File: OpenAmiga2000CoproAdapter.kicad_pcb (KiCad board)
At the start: 2 copper layers, 188.6 x 110.4 mm, 75 parts, among them CN1 A2000_COPRO_SLOT, P1 CONN_2, P10 CONN_1, P11 CONN_1, P12 CONN_1, P13 CONN_1, P14 CONN_1, P15 CONN_1, P2 CONN_2, P3 CONN_2, P4 CONN_2, P5 CONN_1, P6 CONN_1, P7 CONN_1, P8 CONN_1, P9 CONN_1, P99 OSHW_LOGO, U1 68000D, U10 Spare, U11 74HCT00, U12 74HCT27, U13 74HCT74, U14 74F86, U15 74F74, U16 74HCT04, U17 74HCT112, U18 74F157, U19 74F157, U2 AS6C4008-55PCN, U3 AS6C4008-55PCN, U4 AS6C4008-55PCN, U5 AS6C4008-55PCN, U6 74HCT00, U7 74HCT32, U8 74HCT32, U9 74LS05

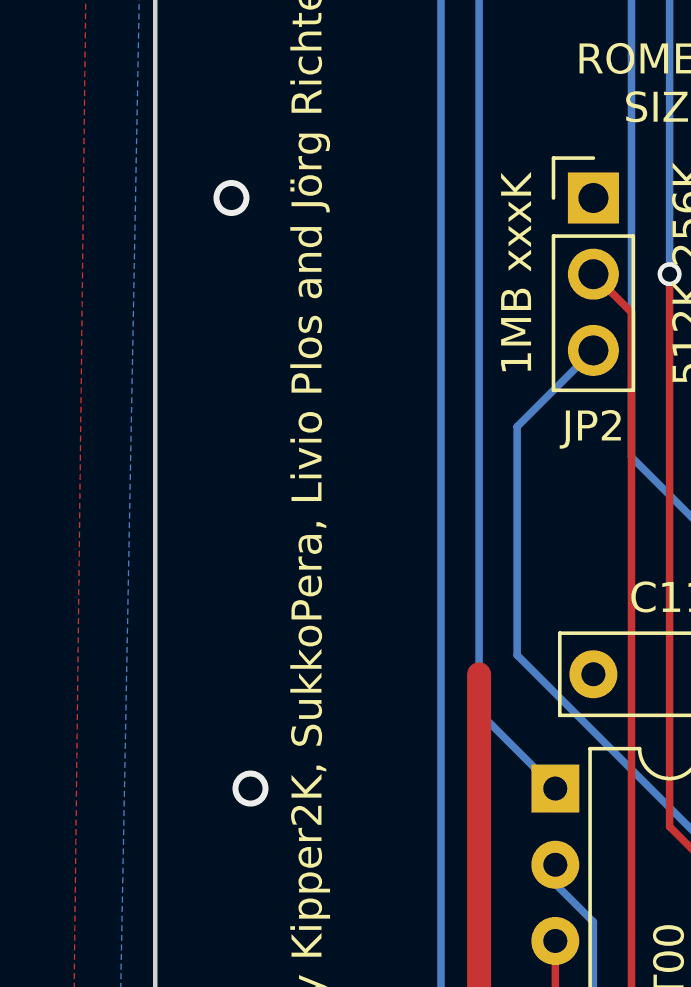
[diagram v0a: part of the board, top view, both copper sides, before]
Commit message: fix unconnected via
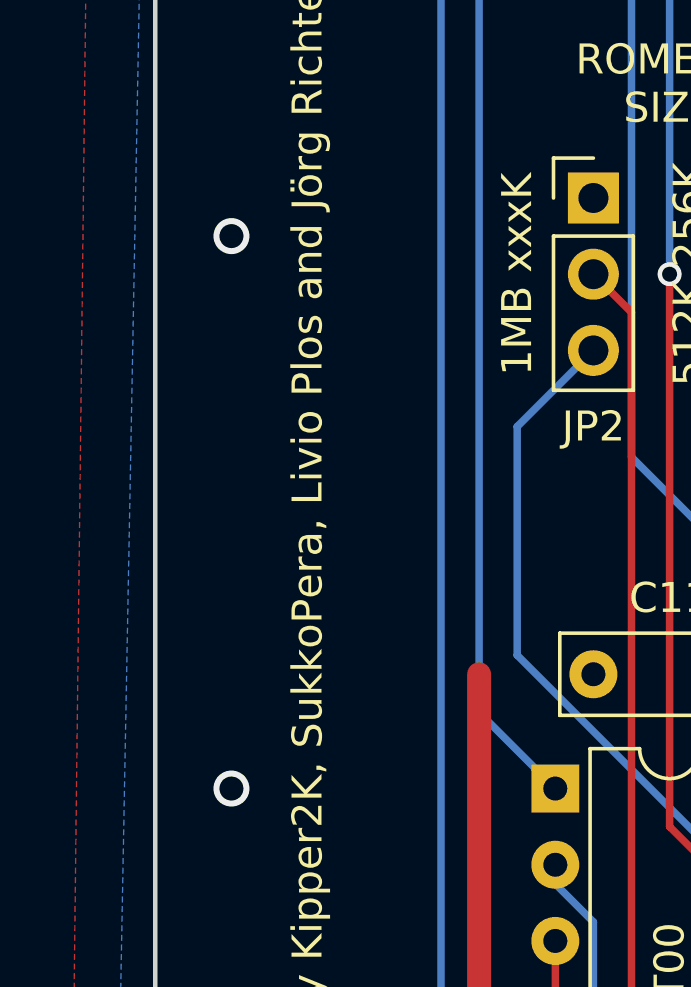
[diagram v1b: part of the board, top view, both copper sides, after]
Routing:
- net GND: vias 173 -> 174
- net (no net): vias 1 -> 0
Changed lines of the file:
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@@
   (gr_line (start 202.3745 139.0015) (end 202.3745 145.9865) (layer Edge.Cuts) (width 0.15))
   (gr_line (start 90.7415 145.9865) (end 90.7415 139.0904) (layer Edge.Cuts) (width 0.15))
-  (via (at 43.7515 72.39) (size 1.2) (drill 0.8) (layers F.Cu B.Cu) (net 0))
   (segment (start 80.8965 50.8) (end 77.7215 47.625) (width 0.25) (layer F.Cu) (net 131))
   (segment (start 82.4865 50.8) (end 80.8965 50.8) (width 0.25) (layer F.Cu) (net 131))
@@
   (via (at 44.3865 137.16) (size 1.2) (drill 0.8) (layers F.Cu B.Cu) (net 1))
   (via (at 44.3865 111.125) (size 1.2) (drill 0.8) (layers F.Cu B.Cu) (net 1))
-  (via (at 44.3865 92.075) (size 1.2) (drill 0.8) (layers F.Cu B.Cu) (net 1))
+  (via (at 43.7515 92.075) (size 1.2) (drill 0.8) (layers F.Cu B.Cu) (net 1))
   (via (at 208.8515 52.705) (size 1.2) (drill 0.8) (layers F.Cu B.Cu) (net 1))
   (via (at 205.0415 57.785) (size 1.2) (drill 0.8) (layers F.Cu B.Cu) (net 1))
@@
   (segment (start 187.2615 122.555) (end 187.2615 127.635) (width 0.8) (layer B.Cu) (net 1))
   (via (at 187.2615 127.635) (size 1.2) (drill 0.8) (layers F.Cu B.Cu) (net 1))
+  (via (at 43.7515 73.66) (size 1.2) (drill 0.8) (layers F.Cu B.Cu) (net 1))
   (segment (start 126.238 108.6485) (end 126.3015 108.585) (width 0.8) (layer F.Cu) (net 2))
   (segment (start 126.238 112.0775) (end 126.238 108.6485) (width 0.8) (layer F.Cu) (net 2))

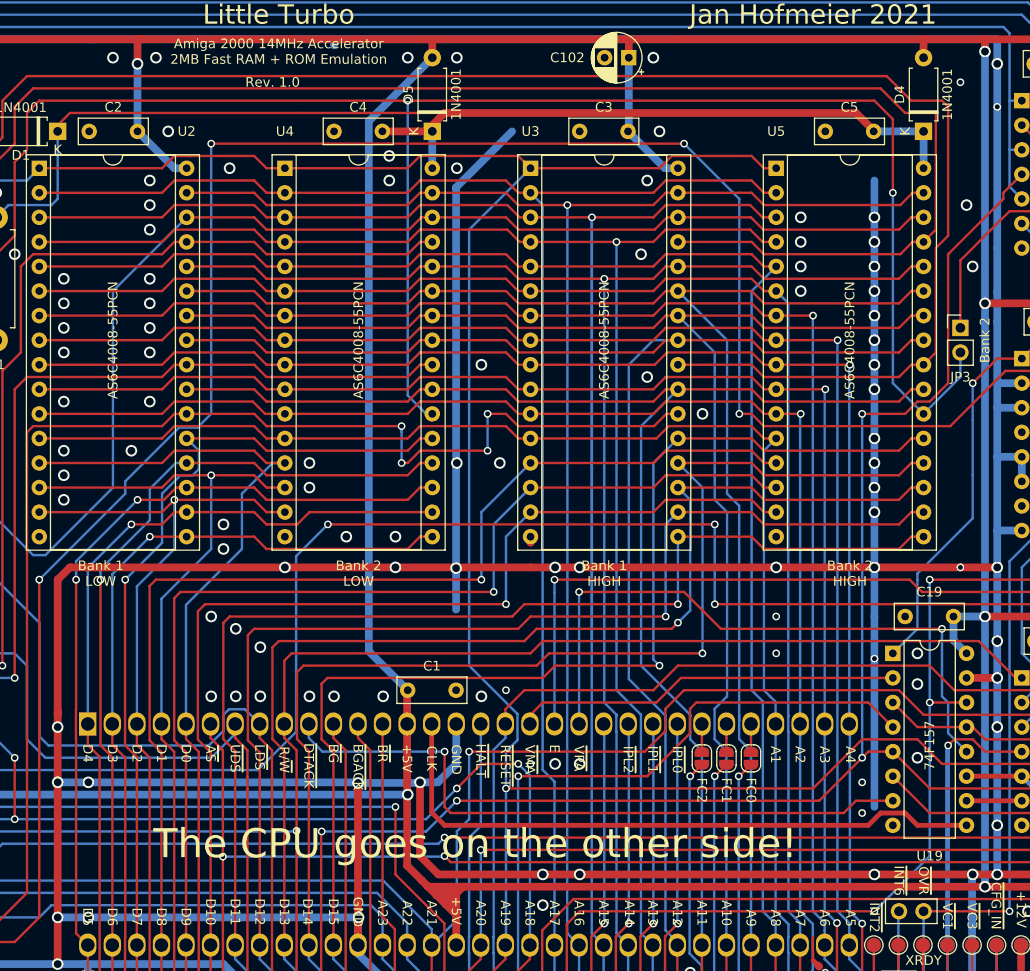
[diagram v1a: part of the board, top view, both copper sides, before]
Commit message: remove a few vias via
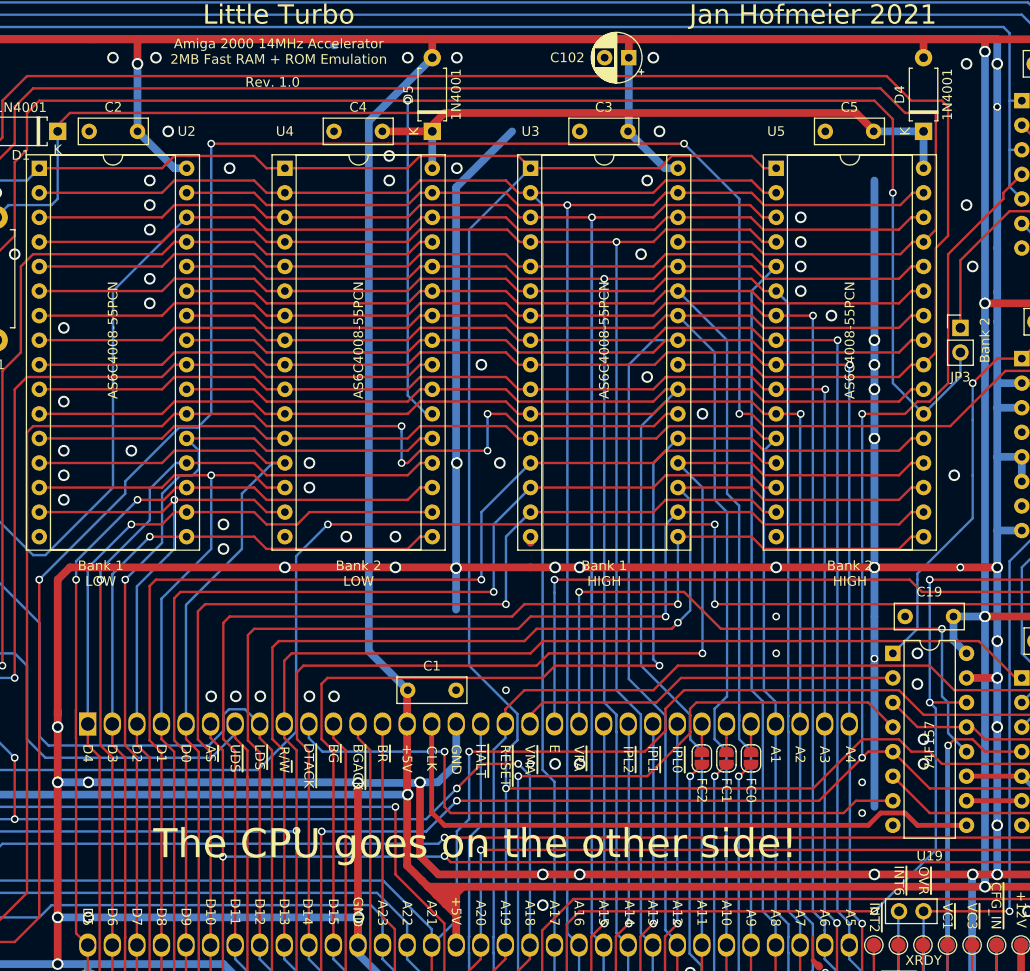
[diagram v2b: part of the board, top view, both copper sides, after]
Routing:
- net /~vpa: track 134.8 -> 135.3 mm
- net GND: vias 174 -> 158
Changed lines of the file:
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@@
     (thickness 1.6)
     (drawings 129)
-    (tracks 2324)
+    (tracks 2311)
     (zones 0)
     (modules 75)
@@
   (via (at 69.7865 111.125) (size 1.2) (drill 0.8) (layers F.Cu B.Cu) (net 1))
   (segment (start 187.2615 103.505) (end 187.2615 103.505) (width 0.8) (layer F.Cu) (net 1))
-  (via (at 187.2615 103.505) (size 1.2) (drill 0.8) (layers F.Cu B.Cu) (net 1))
+  (via (at 187.2615 103.505) (size 1.2) (drill 0.8) (layers F.Cu B.Cu) (net 1) (status 1000000))
   (segment (start 189.8015 86.995) (end 189.8015 84.455) (width 0.8) (layer B.Cu) (net 1))
   (segment (start 187.2615 84.455) (end 189.8015 84.455) (width 0.8) (layer B.Cu) (net 1))
@@
   (via (at 100.2665 43.18) (size 1.2) (drill 0.8) (layers F.Cu B.Cu) (net 1))
   (via (at 166.9415 59.69) (size 1.2) (drill 0.8) (layers F.Cu B.Cu) (net 1))
-  (via (at 174.5615 59.69) (size 1.2) (drill 0.8) (layers F.Cu B.Cu) (net 1))
   (via (at 166.9415 62.23) (size 1.2) (drill 0.8) (layers F.Cu B.Cu) (net 1))
-  (via (at 174.5615 62.23) (size 1.2) (drill 0.8) (layers F.Cu B.Cu) (net 1))
-  (via (at 174.5615 64.77) (size 1.2) (drill 0.8) (layers F.Cu B.Cu) (net 1))
   (via (at 166.9415 64.77) (size 1.2) (drill 0.8) (layers F.Cu B.Cu) (net 1))
   (via (at 166.9415 67.31) (size 1.2) (drill 0.8) (layers F.Cu B.Cu) (net 1))
-  (via (at 174.5615 67.31) (size 1.2) (drill 0.8) (layers F.Cu B.Cu) (net 1))
-  (via (at 174.5615 69.85) (size 1.2) (drill 0.8) (layers F.Cu B.Cu) (net 1))
+  (via (at 170.1165 69.85) (size 1.2) (drill 0.8) (layers F.Cu B.Cu) (net 1))
   (via (at 174.5615 72.39) (size 1.2) (drill 0.8) (layers F.Cu B.Cu) (net 1))
   (via (at 174.5615 74.93) (size 1.2) (drill 0.8) (layers F.Cu B.Cu) (net 1))
   (via (at 174.5615 77.47) (size 1.2) (drill 0.8) (layers F.Cu B.Cu) (net 1))
-  (via (at 174.5615 82.55) (size 1.2) (drill 0.8) (layers F.Cu B.Cu) (net 1))
-  (via (at 174.5615 85.09) (size 1.2) (drill 0.8) (layers F.Cu B.Cu) (net 1))
-  (via (at 174.5615 87.63) (size 1.2) (drill 0.8) (layers F.Cu B.Cu) (net 1))
-  (via (at 174.5615 90.17) (size 1.2) (drill 0.8) (layers F.Cu B.Cu) (net 1))
+  (via (at 182.8165 86.36) (size 1.2) (drill 0.8) (layers F.Cu B.Cu) (net 1))
   (via (at 85.6615 63.5) (size 1.2) (drill 0.8) (layers F.Cu B.Cu) (net 1))
   (via (at 78.0415 97.155) (size 1.2) (drill 0.8) (layers F.Cu B.Cu) (net 1))
   (via (at 118.6815 109.22) (size 1.2) (drill 0.8) (layers F.Cu B.Cu) (net 1))
-  (via (at 123.7615 109.22) (size 1.2) (drill 0.8) (layers F.Cu B.Cu) (net 1))
   (via (at 52.0065 111.125) (size 1.2) (drill 0.8) (layers F.Cu B.Cu) (net 1))
   (via (at 43.7515 54.61) (size 1.2) (drill 0.8) (layers F.Cu B.Cu) (net 1))
@@
   (segment (start 168.2115 136.525) (end 168.2115 135.763425) (width 0.25) (layer F.Cu) (net 1))
   (segment (start 168.2115 135.763425) (end 168.19299 135.744915) (width 0.25) (layer F.Cu) (net 1))
-  (via (at 111.0615 104.14) (size 1.2) (drill 0.8) (layers F.Cu B.Cu) (net 1))
   (via (at 111.0615 109.22) (size 1.2) (drill 0.8) (layers F.Cu B.Cu) (net 1))
-  (via (at 108.5215 102.235) (size 1.2) (drill 0.8) (layers F.Cu B.Cu) (net 1))
   (via (at 108.5215 109.22) (size 1.2) (drill 0.8) (layers F.Cu B.Cu) (net 1))
-  (via (at 105.9815 100.965) (size 1.2) (drill 0.8) (layers F.Cu B.Cu) (net 1))
   (via (at 105.9815 109.22) (size 1.2) (drill 0.8) (layers F.Cu B.Cu) (net 1))
   (via (at 144.0815 95.885) (size 1.2) (drill 0.8) (layers F.Cu B.Cu) (net 1))
@@
   (segment (start 187.2615 48.26) (end 187.2615 62.865) (width 0.8) (layer B.Cu) (net 1))
   (via (at 187.2615 48.26) (size 0.8) (drill 0.5) (layers F.Cu B.Cu) (net 1))
-  (via (at 183.4515 45.72) (size 0.8) (drill 0.5) (layers F.Cu B.Cu) (net 1))
   (via (at 78.0415 57.785) (size 0.8) (drill 0.5) (layers F.Cu B.Cu) (net 1))
   (via (at 65.9765 59.055) (size 0.8) (drill 0.5) (layers F.Cu B.Cu) (net 1))
@@
   (via (at 144.0815 127.635) (size 1.2) (drill 0.8) (layers F.Cu B.Cu) (net 1))
   (via (at 140.2715 130.81) (size 1.2) (drill 0.8) (layers F.Cu B.Cu) (net 1))
-  (via (at 133.9215 109.22) (size 1.2) (drill 0.8) (layers F.Cu B.Cu) (net 1))
   (via (at 213.9315 103.505) (size 1.2) (drill 0.8) (layers F.Cu B.Cu) (net 1))
   (segment (start 213.9315 62.23) (end 213.9315 62.795685) (width 0.8) (layer B.Cu) (net 1))
@@
   (via (at 99.6315 66.04) (size 1.2) (drill 0.8) (layers F.Cu B.Cu) (net 1))
   (via (at 99.6315 68.58) (size 1.2) (drill 0.8) (layers F.Cu B.Cu) (net 1))
-  (via (at 99.6315 71.12) (size 1.2) (drill 0.8) (layers F.Cu B.Cu) (net 1))
-  (via (at 99.6315 73.66) (size 1.2) (drill 0.8) (layers F.Cu B.Cu) (net 1))
-  (via (at 99.6315 78.74) (size 1.2) (drill 0.8) (layers F.Cu B.Cu) (net 1))
   (via (at 97.7265 83.82) (size 1.2) (drill 0.8) (layers F.Cu B.Cu) (net 1))
-  (via (at 90.7415 66.04) (size 1.2) (drill 0.8) (layers F.Cu B.Cu) (net 1))
-  (via (at 90.7415 68.58) (size 1.2) (drill 0.8) (layers F.Cu B.Cu) (net 1))
   (via (at 90.7415 71.12) (size 1.2) (drill 0.8) (layers F.Cu B.Cu) (net 1))
-  (via (at 90.7415 73.66) (size 1.2) (drill 0.8) (layers F.Cu B.Cu) (net 1))
   (via (at 90.7415 78.74) (size 1.2) (drill 0.8) (layers F.Cu B.Cu) (net 1))
   (via (at 90.7415 83.82) (size 1.2) (drill 0.8) (layers F.Cu B.Cu) (net 1))
@@
   (via (at 179.0065 107.95) (size 1.2) (drill 0.8) (layers F.Cu B.Cu) (net 1))
   (via (at 187.2615 112.395) (size 1.2) (drill 0.8) (layers F.Cu B.Cu) (net 1))
-  (via (at 179.0065 115.57) (size 1.2) (drill 0.8) (layers F.Cu B.Cu) (net 1))
+  (via (at 179.6415 116.205) (size 1.2) (drill 0.8) (layers F.Cu B.Cu) (net 1))
   (segment (start 174.5615 120.65) (end 174.5615 105.31999) (width 0.8) (layer B.Cu) (net 1))
   (segment (start 217.7415 103.505) (end 217.7415 100.33) (width 0.8) (layer B.Cu) (net 1))
@@
   (via (at 187.2615 127.635) (size 1.2) (drill 0.8) (layers F.Cu B.Cu) (net 1))
   (via (at 43.7515 73.66) (size 1.2) (drill 0.8) (layers F.Cu B.Cu) (net 1))
+  (via (at 174.5615 82.55) (size 1.2) (drill 0.8) (layers F.Cu B.Cu) (net 1))
+  (via (at 184.0865 43.815) (size 1.2) (drill 0.8) (layers F.Cu B.Cu) (net 1))
+  (via (at 179.6415 113.665) (size 1.2) (drill 0.8) (layers F.Cu B.Cu) (net 1))
   (segment (start 126.238 108.6485) (end 126.3015 108.585) (width 0.8) (layer F.Cu) (net 2))
   (segment (start 126.238 112.0775) (end 126.238 108.6485) (width 0.8) (layer F.Cu) (net 2))
@@
   (segment (start 174.5615 131.445012) (end 144.081488 131.445012) (width 0.25) (layer F.Cu) (net 6))
   (segment (start 174.5615 131.445) (end 174.5615 131.445012) (width 0.25) (layer B.Cu) (net 6))
-  (segment (start 180.276538 125.729962) (end 174.5615 131.445) (width 0.25) (layer B.Cu) (net 6))
-  (segment (start 180.276538 109.855) (end 180.276538 125.729962) (width 0.25) (layer B.Cu) (net 6))
+  (segment (start 180.9115 125.095) (end 174.5615 131.445) (width 0.25) (layer B.Cu) (net 6))
+  (segment (start 180.9115 110.489962) (end 180.9115 125.095) (width 0.25) (layer B.Cu) (net 6))
+  (segment (start 180.276538 109.855) (end 180.9115 110.489962) (width 0.25) (layer B.Cu) (net 6))
   (segment (start 140.208 133.4135) (end 143.4465 130.175) (width 0.25) (layer F.Cu) (net 7))
   (segment (start 143.4465 130.175) (end 192.9765 130.175) (width 0.25) (layer F.Cu) (net 7))
@@
   (segment (start 63.4365 55.88) (end 58.3565 60.96) (width 0.25) (layer B.Cu) (net 11))
   (segment (start 86.9315 55.88) (end 63.4365 55.88) (width 0.25) (layer B.Cu) (net 11))
+  (segment (start 173.2915 113.665) (end 168.2115 118.745) (width 0.25) (layer F.Cu) (net 11))
+  (segment (start 177.1015 113.665) (end 173.2915 113.665) (width 0.25) (layer F.Cu) (net 11))
+  (segment (start 178.3715 114.935) (end 177.1015 113.665) (width 0.25) (layer F.Cu) (net 11))
+  (segment (start 180.2765 114.935) (end 178.3715 114.935) (width 0.25) (layer F.Cu) (net 11))
+  (segment (start 181.5465 116.205) (end 180.2765 114.935) (width 0.25) (layer F.Cu) (net 11))
   (segment (start 168.2115 118.745) (end 136.4615 118.745) (width 0.25) (layer F.Cu) (net 11))
-  (segment (start 179.0065 113.665) (end 173.2915 113.665) (width 0.25) (layer F.Cu) (net 11))
-  (segment (start 181.5465 116.205) (end 179.0065 113.665) (width 0.25) (layer F.Cu) (net 11))
   (segment (start 193.6115 116.205) (end 181.5465 116.205) (width 0.25) (layer F.Cu) (net 11))
-  (segment (start 173.2915 113.665) (end 168.2115 118.745) (width 0.25) (layer F.Cu) (net 11))
   (segment (start 197.4215 112.395) (end 193.6115 116.205) (width 0.25) (layer F.Cu) (net 11))
   (segment (start 131.318 139.1845) (end 131.318 142.6845) (width 0.25) (layer F.Cu) (net 12) (status 20))
